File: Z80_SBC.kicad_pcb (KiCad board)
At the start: 2 copper layers, 100 x 100 mm, 10 parts, among them U1 Z80CPU, U2 HM62256BLP, U3 27C64, U4 74HCT04, U5 74LS139, Y1 1.8432MHz

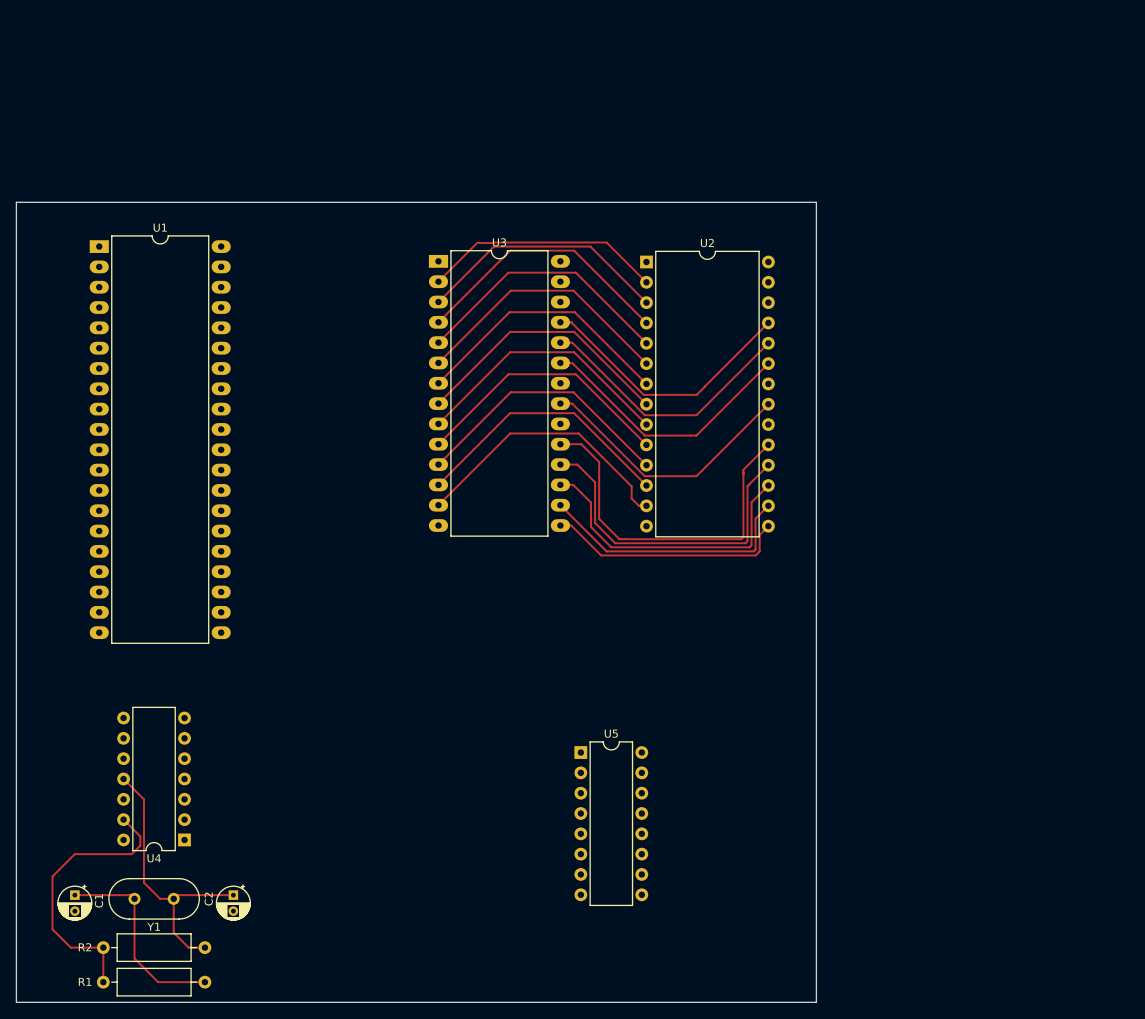
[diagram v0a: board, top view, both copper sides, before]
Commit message: added 6850 USART
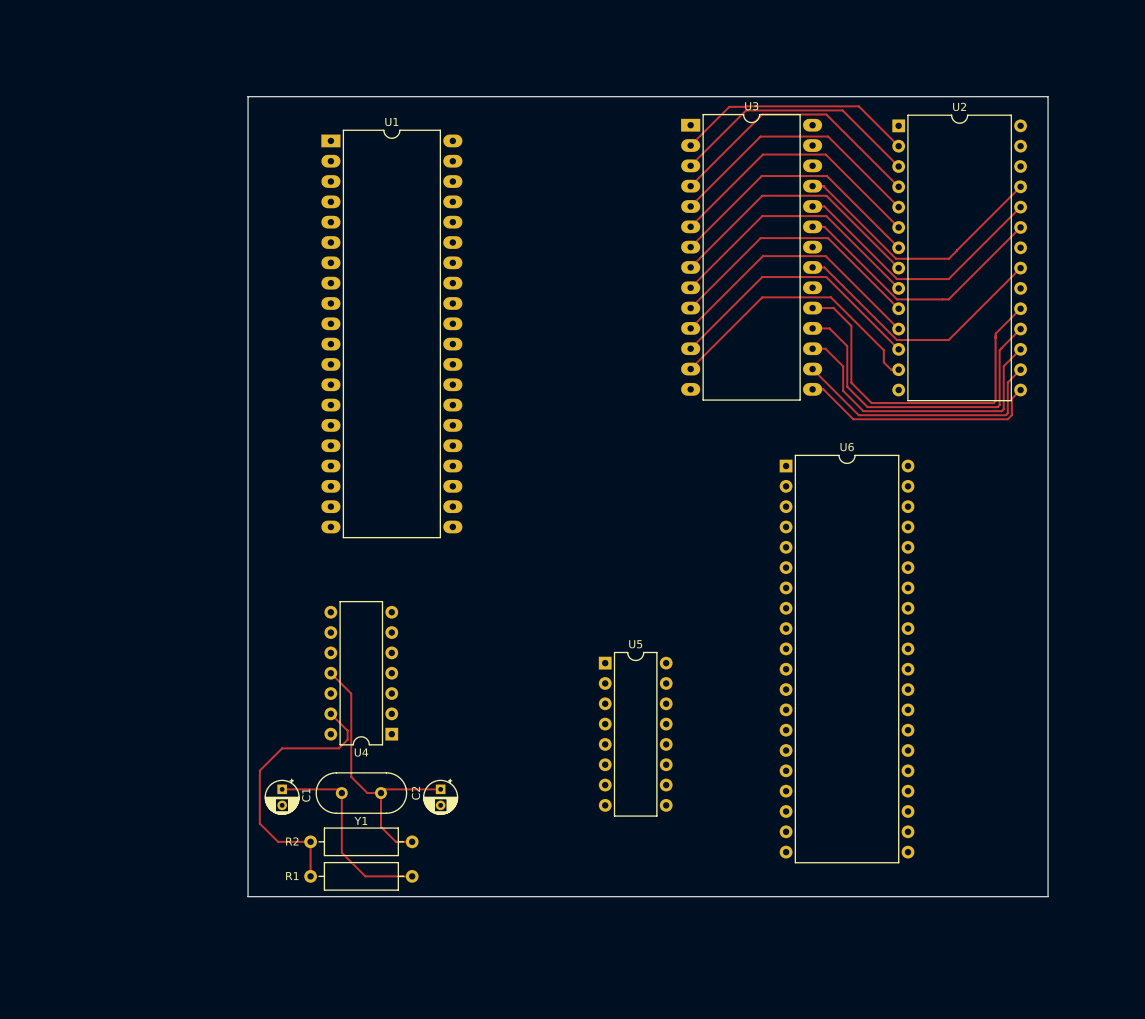
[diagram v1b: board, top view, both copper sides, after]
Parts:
- added U6: MC68A50, Package_DIP:DIP-40_W15.24mm, F.Cu at (156.2, 93.0)
- moved U2 35.8 mm to (170.3, 50.4)
- moved U3 35.8 mm to (144.3, 50.4)
- moved U1 31.8 mm to (99.3, 52.3)
- moved C1 29.1 mm to (93.2, 133.4)
- moved C2 29.1 mm to (113.0, 133.4)
- moved R2 29.1 mm to (109.5, 139.9)
- moved U4 29.1 mm to (106.9, 126.5)
- moved Y1 29.1 mm to (105.6, 133.8)
- moved R1 29.1 mm to (96.8, 144.3)
- moved U5 11.6 mm to (133.6, 117.6)
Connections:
- U1 pad 21: unconnected-(U1-~{RD}-Pad21) -> ~{RD}
- U1 pad 22: unconnected-(U1-~{WR}-Pad22) -> ~{WR}
- U2 pad 22: unconnected-(U2-~{OE}-Pad22) -> ~{RD}
- U2 pad 27: unconnected-(U2-~{WE}-Pad27) -> ~{WR}
- U3 pad 22: unconnected-(U3-~{OE}-Pad22) -> ~{RD}
- U4 pad 1: Net-(U5A-E) -> /Address15
- U5 pad 1: Net-(U5A-E) -> /Address15

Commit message: poor route
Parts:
- added C10: 0.1uF, Capacitor_THT:C_Radial_D4.0mm_H5.0mm_P1.50mm, F.Cu at (188.0, 39.1)
- added C11: 0.1uF, Capacitor_THT:C_Radial_D4.0mm_H5.0mm_P1.50mm, F.Cu at (161.8, 39.1)
- added C3: 100uF, Capacitor_THT:CP_Radial_D4.0mm_P1.50mm, F.Cu at (111.8, 42.2)
- added C4: 0.1uF, Capacitor_THT:C_Radial_D4.0mm_H5.0mm_P1.50mm, F.Cu at (129.3, 93.5)
- added C5: 0.1uF, Capacitor_THT:C_Radial_D4.0mm_H5.0mm_P1.50mm, F.Cu at (139.4, 113.8)
- added C6: 0.1uF, Capacitor_THT:C_Radial_D4.0mm_H5.0mm_P1.50mm, F.Cu at (190.5, 97.8)
- added C7: 0.1uF, Capacitor_THT:C_Radial_D4.0mm_H5.0mm_P1.50mm, F.Cu at (126.2, 102.1)
- added C8: 0.1uF, Capacitor_THT:C_Radial_D4.0mm_H5.0mm_P1.50mm, F.Cu at (113.0, 97.5)
- added C9: 0.1uF, Capacitor_THT:C_Radial_D4.0mm_H5.0mm_P1.50mm, F.Cu at (190.8, 119.1)
- added D1: LED, LED_THT:LED_D3.0mm, F.Cu at (154.4, 131.3)
- added D2: LED, LED_THT:LED_D3.0mm, F.Cu at (160.3, 131.3)
- added D3: LED, LED_THT:LED_D3.0mm, F.Cu at (166.1, 131.3)
- added D4: LED, LED_THT:LED_D3.0mm, F.Cu at (171.9, 131.3)
- added D5: LED, LED_THT:LED_D3.0mm, F.Cu at (177.8, 131.3)
- added D6: LED, LED_THT:LED_D3.0mm, F.Cu at (183.6, 131.3)
- added D7: LED, LED_THT:LED_D3.0mm, F.Cu at (189.5, 131.1)
- added D8: LED, LED_THT:LED_D3.0mm, F.Cu at (195.3, 131.1)
- added J1: USB_C_Receptacle_PowerOnly_6P, Connector_USB:USB_C_Receptacle_GCT_USB4125-xx-x_6P_TopMnt_Horizontal, F.Cu at (101.8, 43.7)
- added J2: Conn_01x04_Pin, Connector_PinHeader_1.27mm:PinHeader_1x04_P1.27mm_Vertical, F.Cu at (196.6, 91.2)
- added R4: 3k3, Resistor_THT:R_Axial_DIN0309_L9.0mm_D3.2mm_P12.70mm_Horizontal, F.Cu at (102.8, 113.8)
- added RN1: R_Network08, Resistor_THT:R_Array_SIP9, F.Cu at (189.5, 135.4)
- added U7: 74LS573, Package_DIP:DIP-20_W7.62mm, F.Cu at (186.9, 115.8)
- added U8: 74LS32, Package_DIP:DIP-14_W7.62mm, F.Cu at (135.1, 118.4)
- U6: footprint Package_DIP:DIP-40_W15.24mm -> Package_DIP:DIP-24_W15.24mm
- moved U6 30.3 mm to (186.4, 90.7), turned to -90 degrees
- moved U1 25.0 mm to (121.2, 40.1)
- moved U4 24.7 mm to (108.4, 101.8), turned to 0 degrees
- moved C1 13.3 mm to (102.6, 124.0)
- moved C2 13.3 mm to (122.4, 124.0)
- moved R1 13.3 mm to (106.2, 134.9)
- moved R2 13.3 mm to (118.9, 130.5)
- moved Y1 13.3 mm to (115.0, 124.4)
- moved U3 11.5 mm to (154.1, 44.4)
- moved U2 11.5 mm to (180.1, 44.5)
- moved U5 11.3 mm to (130.8, 106.7), turned to 90 degrees
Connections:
- U1 pad 11: unconnected-(U1-VCC-Pad11) -> 5V
- U1 pad 16: unconnected-(U1-~{INT}-Pad16) -> ~{INT}
- U1 pad 17: unconnected-(U1-~{NMI}-Pad17) -> 5V
- U1 pad 19: unconnected-(U1-~{MREQ}-Pad19) -> ~{MREQ}
- U1 pad 20: unconnected-(U1-~{IORQ}-Pad20) -> ~{I/O}
- U1 pad 24: unconnected-(U1-~{WAIT}-Pad24) -> 5V
- U1 pad 25: unconnected-(U1-~{BUSRQ}-Pad25) -> 5V
- U1 pad 27: unconnected-(U1-~{M1}-Pad27) -> ~{M1}
- U1 pad 30: /Address0 -> A0
- U1 pad 36: /Address6 -> A6
- U1 pad 37: /Address7 -> A7
- U2 pad 10: /Address0 -> A0
- U2 pad 22: ~{RD} -> ~{MEMRD}
- U2 pad 27: ~{WR} -> ~{MEMWR}
- U2 pad 28: unconnected-(U2-VCC-Pad28) -> 5V
- U2 pad 3: /Address7 -> A7
- U2 pad 4: /Address6 -> A6
- U3 pad 10: /Address0 -> A0
- U3 pad 22: ~{RD} -> ~{MEMRD}
- U3 pad 27: unconnected-(U3-~{WE}-Pad27) -> 5V
- U3 pad 28: unconnected-(U3-VCC-Pad28) -> 5V
- U3 pad 3: /Address7 -> A7
- U3 pad 4: /Address6 -> A6
- U4 pad 14: Net-(U4G-VCC) -> 5V
- U4 pad 3: GND -> ~{I/O}
- U4 pad 4: GND -> Net-(U6-E)
- U4 pad 5: GND -> Net-(U5A-O1)
- U4 pad 6: GND -> Net-(U7-Load)
- U5 pad 16: Net-(U4G-VCC) -> 5V
- U5 pad 5: unconnected-(U5A-O1-Pad5) -> Net-(U5A-O1)
- U6 pad 10: unconnected-(U6-CS1-Pad10) -> A6
- U6 pad 11: unconnected-(U6-RS-Pad11) -> A0
- U6 pad 12: unconnected-(U6-VCC-Pad12) -> 5V
- U6 pad 13: unconnected-(U6-R/~{W}-Pad13) -> ~{WR}
- U6 pad 14: unconnected-(U6-E-Pad14) -> Net-(U6-E)
- U6 pad 2: unconnected-(U6-Rx_Data-Pad2) -> RX
- U6 pad 23: unconnected-(U6-~{DCD}-Pad23) -> GND
- U6 pad 24: unconnected-(U6-~{CTS}-Pad24) -> GND
- U6 pad 3: unconnected-(U6-Rx_CLK-Pad3) -> CLK
- U6 pad 4: unconnected-(U6-Tx_CLK-Pad4) -> CLK
- U6 pad 6: unconnected-(U6-Tx_Data-Pad6) -> TX
- U6 pad 7: unconnected-(U6-~{IRQ}-Pad7) -> ~{INT}
- U6 pad 8: unconnected-(U6-CS0-Pad8) -> ~{M1}
- U6 pad 9: unconnected-(U6-CS2-Pad9) -> A7
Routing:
- net GND: track 0.00 -> 516.5 mm, vias 0 -> 22
- net 5V: track 0.00 -> 439.3 mm, vias 0 -> 6
- net A13: track 0.00 -> 171.7 mm, vias 0 -> 3
- net A14: track 0.00 -> 158.8 mm
- net CLK: track 0.00 -> 148.6 mm, vias 0 -> 5
- net /Data0: track 33.5 -> 172.1 mm, vias 0 -> 2
- net /Data2: track 34.3 -> 171.4 mm, vias 0 -> 3
- net /Data1: track 33.5 -> 165.4 mm
- net ~{MEMRD}: track 0.00 -> 119.8 mm, vias 0 -> 2
- net /Data3: track 30.6 -> 149.4 mm, vias 0 -> 3
- net ~{MEMWR}: track 0.00 -> 118.5 mm, vias 0 -> 2
- net /Data4: track 33.0 -> 150.0 mm, vias 0 -> 2
- net /Data5: track 37.4 -> 150.9 mm, vias 0 -> 2
- net /Data6: track 41.1 -> 153.2 mm, vias 0 -> 3
- net Net-(U2-~{CS}): track 0.00 -> 106.7 mm, vias 0 -> 4
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
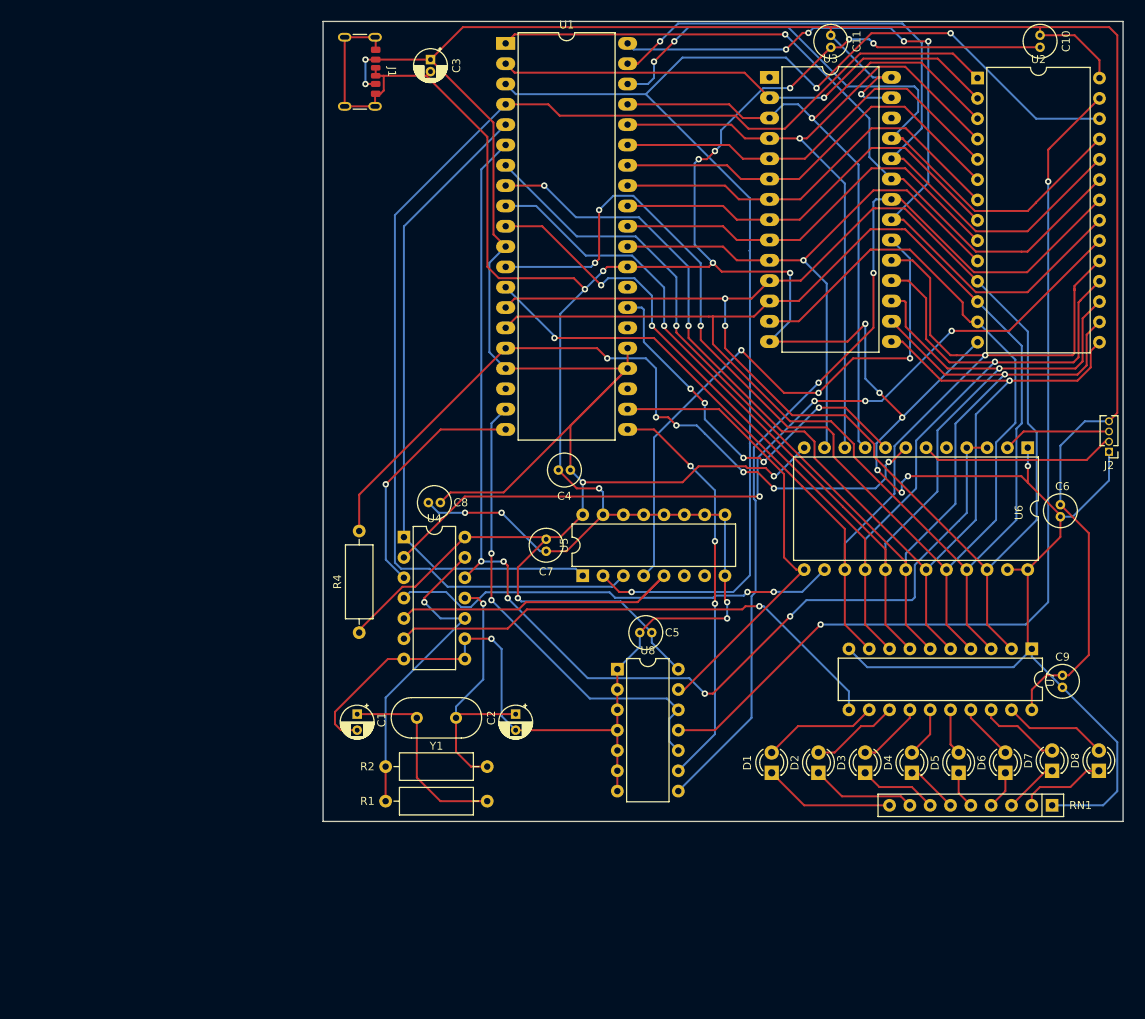
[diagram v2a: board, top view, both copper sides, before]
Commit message: fix DRC errors and warning, add reset and power
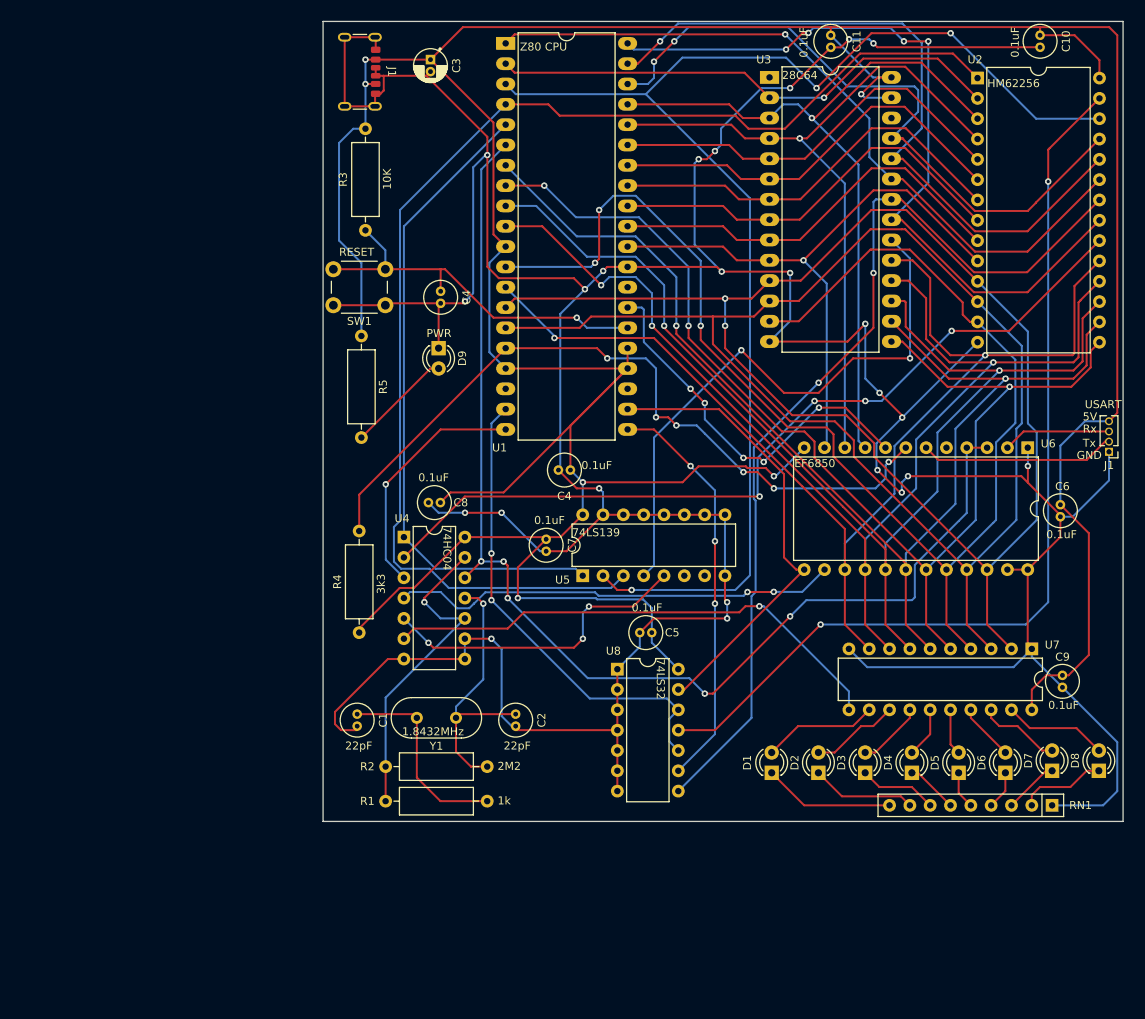
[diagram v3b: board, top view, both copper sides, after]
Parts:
- added C4: 0.1uF, Capacitor_THT:C_Radial_D4.0mm_H5.0mm_P1.50mm, F.Cu at (113.0, 71.1)
- added D9: LED, LED_THT:LED_D3.0mm, F.Cu at (112.8, 78.2)
- added R3: 10K, Resistor_THT:R_Axial_DIN0309_L9.0mm_D3.2mm_P12.70mm_Horizontal, F.Cu at (103.6, 50.8)
- added R5: 3k3, Resistor_THT:R_Axial_DIN0309_L9.0mm_D3.2mm_P12.70mm_Horizontal, F.Cu at (103.1, 76.7)
- added SW1: SW_Push, Button_Switch_THT:SW_PUSH_6mm, F.Cu at (106.1, 72.9)
- C1, C2: footprint Capacitor_THT:CP_Radial_D4.0mm_P2.00mm -> Capacitor_THT:C_Radial_D4.0mm_H5.0mm_P1.50mm
- renumbered J2 to J1
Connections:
- U1 pad 26: unconnected-(U1-~{RESET}-Pad26) -> Net-(U1-~{RESET})
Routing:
- net Net-(U1-~{RESET}): track 0.00 -> 48.5 mm, vias 0 -> 1
- net GND: track 516.5 -> 560.0 mm, vias 22 -> 24
- net 5V: track 439.3 -> 476.2 mm
- net Net-(D9-A): track 0.00 -> 13.2 mm
- net Net-(U5A-O1): track 38.6 -> 39.7 mm, vias 0 -> 3
- net A13: track 171.7 -> 170.9 mm
- net ROM: vias 3 -> 2
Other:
- board text added: "0.1uF"
- board text added: "1.8432MHz"
- board text added: "10K"
- board text added: "1k"
- board text added: "22pF"
- board text added: "28C64"
- board text added: "2M2"
- board text added: "3k3"
- board text added: "5V"
- board text added: "74HC04"
- board text added: "74LS139"
- board text added: "74LS32"
- board text added: "EF6850"
- board text added: "GND"
- board text added: "HM62256"
- board text added: "PWR"
- board text added: "RESET"
- board text added: "Rx"
- board text added: "Tx"
- board text added: "USART"
- board text added: "Z80 CPU"
- board text added: "Z80 Single Board Computer 8K ROM/32K RAM USART Sebastijan Martincic, 2023"

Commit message: minor fixes
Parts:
- removed the C4 at (129.3, 93.5)
- removed the C4 at (113.0, 71.1)
- added C12: 0.1uF, Capacitor_THT:C_Radial_D4.0mm_H5.0mm_P1.50mm, F.Cu at (112.8, 71.1)
- added C4: 0.1uF, Capacitor_THT:C_Radial_D4.0mm_H5.0mm_P1.50mm, F.Cu at (129.5, 93.5)
- C1, C2: footprint Capacitor_THT:C_Radial_D4.0mm_H5.0mm_P1.50mm -> Capacitor_THT:CP_Radial_D4.0mm_P2.00mm
- R4: value 3k3 -> 10k
- renumbered J1 to J2
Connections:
- U4 pad 8: GND -> unconnected-(U4-Pad8)
- U5 pad 10: GND -> unconnected-(U5B-O2-Pad10)
- U5 pad 11: GND -> unconnected-(U5B-O1-Pad11)
- U5 pad 12: GND -> unconnected-(U5B-O0-Pad12)
- U5 pad 9: GND -> unconnected-(U5B-O3-Pad9)
- U8 pad 3: GND -> unconnected-(U8-Pad3)
- U8 pad 6: GND -> unconnected-(U8-Pad6)
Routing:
- net GND: track 560.0 -> 566.3 mm, vias 24 -> 27
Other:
- board text added: "10k"
- board text removed: "3k3"
